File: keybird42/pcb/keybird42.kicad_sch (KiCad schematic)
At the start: 182 parts, among them SW1 SW_Push, SW10 SW_Push, SW11 SW_Push, SW12 SW_Push, SW13 SW_Push, SW14 SW_Push, SW15 SW_Push, SW16 SW_Push, SW17 SW_Push, SW18 SW_Push, SW19 SW_Push, SW2 SW_Push, SW20 SW_Push, SW21 SW_Push, SW22 SW_Push, SW23 SW_Push, SW24 SW_Push, SW25 SW_Push, SW26 SW_Push, SW27 SW_Push, SW28 SW_Push, SW29 SW_Push, SW3 SW_Push, SW30 SW_Push, SW31 SW_Push, SW32 SW_Push, SW33 SW_Push, SW34 SW_Push, SW35 SW_Push, SW36 SW_Push, SW37 SW_Push, SW38 SW_Push, SW39 SW_Push, SW4 SW_Push, SW40 SW_Push, SW41 SW_Push, SW42 SW_Push, SW43 SW_Push, SW44 SW_Push, SW45 SW_Push, SW46 SW_Push, SW47 SW_Push, SW48 SW_Push, SW49 SW_Push, SW5 SW_Push, SW50 SW_Push, SW51 SW_Push, SW52 SW_Push, SW53 SW_Push, SW54 SW_Push, SW55 SW_Push, SW56 SW_Push, SW57 SW_Push, SW58 SW_Push, SW59 SW_Push, SW6 SW_Push, SW60 SW_Push, SW61 SW_Push, SW62 SW_Push, SW63 SW_Push, SW64 SW_Push, SW65 SW_Push, SW66 SW_Push, SW67 SW_Push, SW68 SW_Push, SW69 SW_Push, SW7 SW_Push, SW70 SW_Push, SW71 SW_Push, SW72 SW_Push, SW73 SW_Push, SW74 SW_Push, SW75 SW_Push, SW76 SW_Push, SW77 SW_Push, SW78 SW_Push, SW79 SW_Push, SW8 SW_Push, SW80 SW_Push, SW81 SW_Push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

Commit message: add rp2040-tiny, fix subdir name
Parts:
- added U1: RP2040-Tiny, symbol keybird42:RP2040-Tiny
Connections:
- net COL1: now also U1.13 (GPIO13)
- net COL2: now also U1.14 (GPIO14)
- net COL3: now also U1.15 (GPIO15)
- net COL4: now also U1.16 (GPIO26)
- net COL5: now also U1.17 (GPIO27)
- net COL6: now also U1.18 (GPIO28)
- net COL7: now also U1.19 (GPIO29)
- net ROWa: now also U1.0 (GPIO0)
- net ROWb: now also U1.1 (GPIO1)
- net ROWc: now also U1.2 (GPIO2)
- net ROWd: now also U1.3 (GPIO3)
- net ROWe: now also U1.4 (GPIO4)
- net ROWf: now also U1.5 (GPIO5)
- net ROWg: now also U1.6 (GPIO6)
- net ROWh: now also U1.7 (GPIO7)
- net ROWi: now also U1.8 (GPIO8)
- net ROWj: now also U1.9 (GPIO9)
- net ROWk: now also U1.10 (GPIO10)
- net ROWl: now also U1.11 (GPIO11)
- net ROWm: now also U1.12 (GPIO12)
- new net GND: U1.21 (GND)
- no-connect marks 0 -> 2
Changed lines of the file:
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@@
   (junction (at 46.99 81.28) (diameter 0) (color 0 0 0 0)
   )
+  (no_connect (at 33.02 246.38))
+  (no_connect (at 33.02 236.22))
   (wire (pts (xy 113.03 127) (xy 127 127))
     (stroke (width 0) (type default))
@@
     (stroke (width 0) (type default))
   )
+  (label "ROWd" (at 55.88 224.79 0) (fields_autoplaced)
+    (effects (font (size 1.27 1.27)) (justify left bottom))
+  )
   (label "ROWj" (at 25.4 139.7 180) (fields_autoplaced)
     (effects (font (size 1.27 1.27)) (justify right bottom))
@@
     (effects (font (size 1.27 1.27)) (justify right bottom))
   )
+  (label "ROWl" (at 55.88 245.11 0) (fields_autoplaced)
+    (effects (font (size 1.27 1.27)) (justify left bottom))
+  )
   (label "COL2" (at 46.99 185.42 270) (fields_autoplaced)
     (effects (font (size 1.27 1.27)) (justify right bottom))
@@
     (effects (font (size 1.27 1.27)) (justify right bottom))
   )
+  (label "ROWe" (at 55.88 227.33 0) (fields_autoplaced)
+    (effects (font (size 1.27 1.27)) (justify left bottom))
+  )
   (label "ROWd" (at 25.4 63.5 180) (fields_autoplaced)
     (effects (font (size 1.27 1.27)) (justify right bottom))
@@
     (effects (font (size 1.27 1.27)) (justify right bottom))
   )
+  (label "ROWm" (at 55.88 247.65 0) (fields_autoplaced)
+    (effects (font (size 1.27 1.27)) (justify left bottom))
+  )
   (label "ROWh" (at 25.4 114.3 180) (fields_autoplaced)
     (effects (font (size 1.27 1.27)) (justify right bottom))
   )
+  (label "COL7" (at 55.88 265.43 0) (fields_autoplaced)
+    (effects (font (size 1.27 1.27)) (justify left bottom))
+  )
+  (label "ROWf" (at 55.88 229.87 0) (fields_autoplaced)
+    (effects (font (size 1.27 1.27)) (justify left bottom))
+  )
   (label "ROWk" (at 25.4 152.4 180) (fields_autoplaced)
     (effects (font (size 1.27 1.27)) (justify right bottom))
@@
     (effects (font (size 1.27 1.27)) (justify right bottom))
   )
+  (label "ROWh" (at 55.88 234.95 0) (fields_autoplaced)
+    (effects (font (size 1.27 1.27)) (justify left bottom))
+  )
   (label "ROWl" (at 25.4 165.1 180) (fields_autoplaced)
     (effects (font (size 1.27 1.27)) (justify right bottom))
@@
     (effects (font (size 1.27 1.27)) (justify right bottom))
   )
+  (label "COL6" (at 55.88 262.89 0) (fields_autoplaced)
+    (effects (font (size 1.27 1.27)) (justify left bottom))
+  )
+  (label "ROWg" (at 55.88 232.41 0) (fields_autoplaced)
+    (effects (font (size 1.27 1.27)) (justify left bottom))
+  )
+  (label "ROWa" (at 55.88 217.17 0) (fields_autoplaced)
+    (effects (font (size 1.27 1.27)) (justify left bottom))
+  )
+  (label "COL5" (at 55.88 260.35 0) (fields_autoplaced)
+    (effects (font (size 1.27 1.27)) (justify left bottom))
+  )
   (label "COL1" (at 33.02 185.42 270) (fields_autoplaced)
     (effects (font (size 1.27 1.27)) (justify right bottom))
@@
     (effects (font (size 1.27 1.27)) (justify right bottom))
   )
+  (label "COL1" (at 55.88 250.19 0) (fields_autoplaced)
+    (effects (font (size 1.27 1.27)) (justify left bottom))
+  )
+  (label "ROWk" (at 55.88 242.57 0) (fields_autoplaced)
+    (effects (font (size 1.27 1.27)) (justify left bottom))
+  )
+  (label "ROWi" (at 55.88 237.49 0) (fields_autoplaced)
+    (effects (font (size 1.27 1.27)) (justify left bottom))
+  )
+  (label "COL2" (at 55.88 252.73 0) (fields_autoplaced)
+    (effects (font (size 1.27 1.27)) (justify left bottom))
+  )
+  (label "COL3" (at 55.88 255.27 0) (fields_autoplaced)
+    (effects (font (size 1.27 1.27)) (justify left bottom))
+  )
+  (label "ROWj" (at 55.88 240.03 0) (fields_autoplaced)
+    (effects (font (size 1.27 1.27)) (justify left bottom))
+  )
+  (label "ROWc" (at 55.88 222.25 0) (fields_autoplaced)
+    (effects (font (size 1.27 1.27)) (justify left bottom))
+  )
   (label "COL3" (at 60.96 185.42 270) (fields_autoplaced)
     (effects (font (size 1.27 1.27)) (justify right bottom))
   )
+  (label "ROWb" (at 55.88 219.71 0) (fields_autoplaced)
+    (effects (font (size 1.27 1.27)) (justify left bottom))
+  )
   (label "COL6" (at 102.87 185.42 270) (fields_autoplaced)
     (effects (font (size 1.27 1.27)) (justify right bottom))
+  )
+  (label "COL4" (at 55.88 257.81 0) (fields_autoplaced)
+    (effects (font (size 1.27 1.27)) (justify left bottom))
   )
   (symbol (lib_id "Diode:1N4148W") (at 113.03 34.29 90) (unit 1)
@@
         )
       )
+    )
+  )
+  (symbol (lib_id "power:GND") (at 33.02 241.3 270) (unit 1)
+    (in_bom yes) (on_board yes) (dnp no) (fields_autoplaced)
+    (property "Reference" "#PWR01" (at 26.67 241.3 0)
+      (effects (font (size 1.27 1.27)) hide)
+    )
+    (property "Value" "GND" (at 29.21 241.3 90)
+      (effects (font (size 1.27 1.27)) (justify right))
+    )
+    (property "Footprint" "" (at 33.02 241.3 0)
+      (effects (font (size 1.27 1.27)) hide)
+    )
+    (property "Datasheet" "" (at 33.02 241.3 0)
+      (effects (font (size 1.27 1.27)) hide)
+    )
+    (pin "1")
+    (instances
+      (project "keybird42"
+        (path "/c6489b6f-cd36-4929-9d41-a438ed9c3e88"
+          (reference "#PWR01") (unit 1)
+        )
+      )
+    )
+  )
+  (symbol (lib_id "keybird42:RP2040-Tiny") (at 44.45 241.3 0) (unit 1)
+    (in_bom yes) (on_board yes) (dnp no) (fields_autoplaced)
+    (property "Reference" "U1" (at 44.45 209.55 0)
+      (effects (font (size 1.27 1.27)))
+    )
+    (property "Value" "RP2040-Tiny" (at 44.45 212.09 0)
+      (effects (font (size 1.27 1.27)))
+    )
+    (property "Footprint" "" (at 44.45 241.3 0)
+      (effects (font (size 1.27 1.27)) hide)
+    )
+    (property "Datasheet" "https://www.waveshare.com/RP2040-Tiny.htm" (at 44.45 269.24 0)
+      (effects (font (size 1.27 1.27)) hide)
+    )
+    (pin "1")
+    (pin "0")
+    (pin "19")
+    (pin "2")
+    (pin "20")
+    (pin "9")
+    (pin "7")
+    (pin "8")
+    (pin "10")
+    (pin "5")
+    (pin "4")
+    (pin "6")
+    (pin "3")
+    (pin "21")
+    (pin "22")
+    (pin "15")
+    (pin "14")
+    (pin "18")
+    (pin "16")
+    (pin "11")
+    (pin "12")
+    (pin "13")
+    (pin "17")
+    (instances
+      (project "keybird42"
+        (path "/c6489b6f-cd36-4929-9d41-a438ed9c3e88"
+          (reference "U1") (unit 1)
+        )
+      )

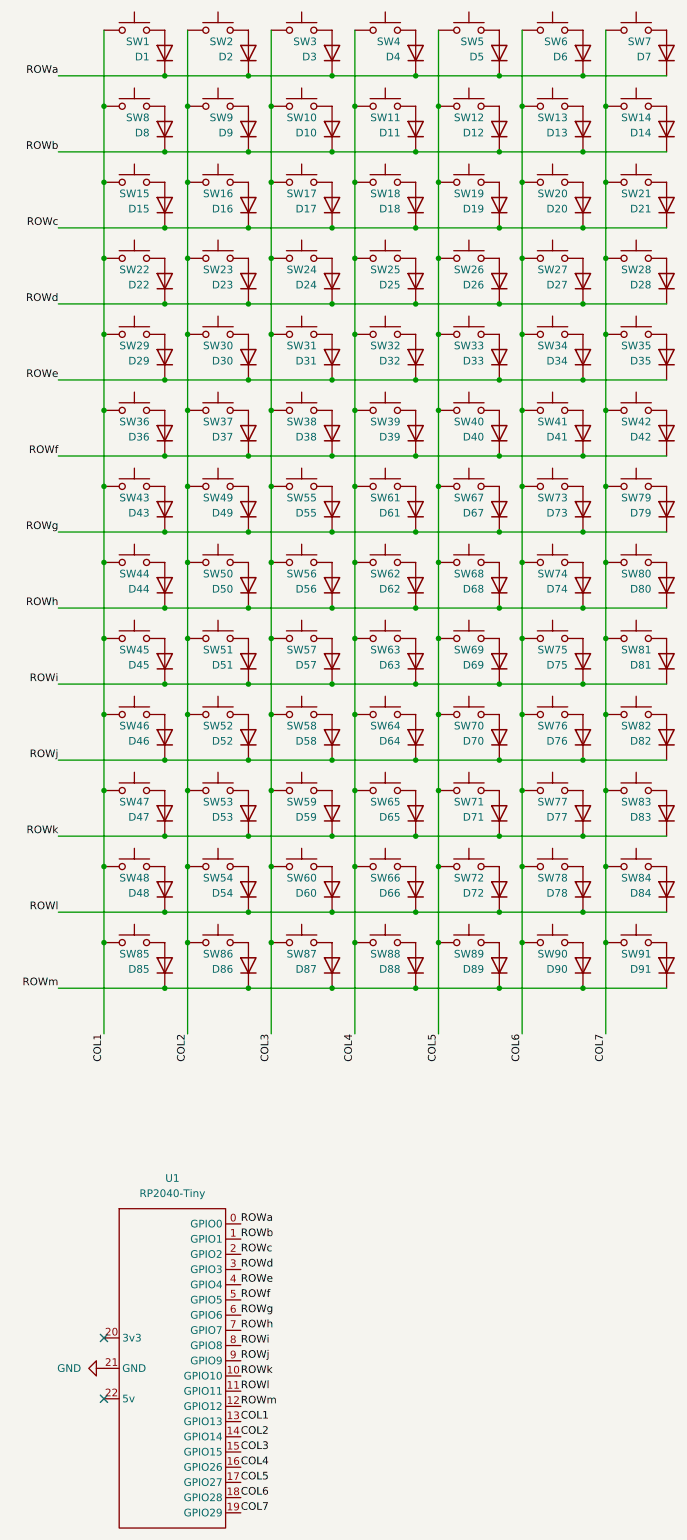
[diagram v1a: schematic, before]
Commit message: update switch and diode symbols; ERC passes; refs are a mess
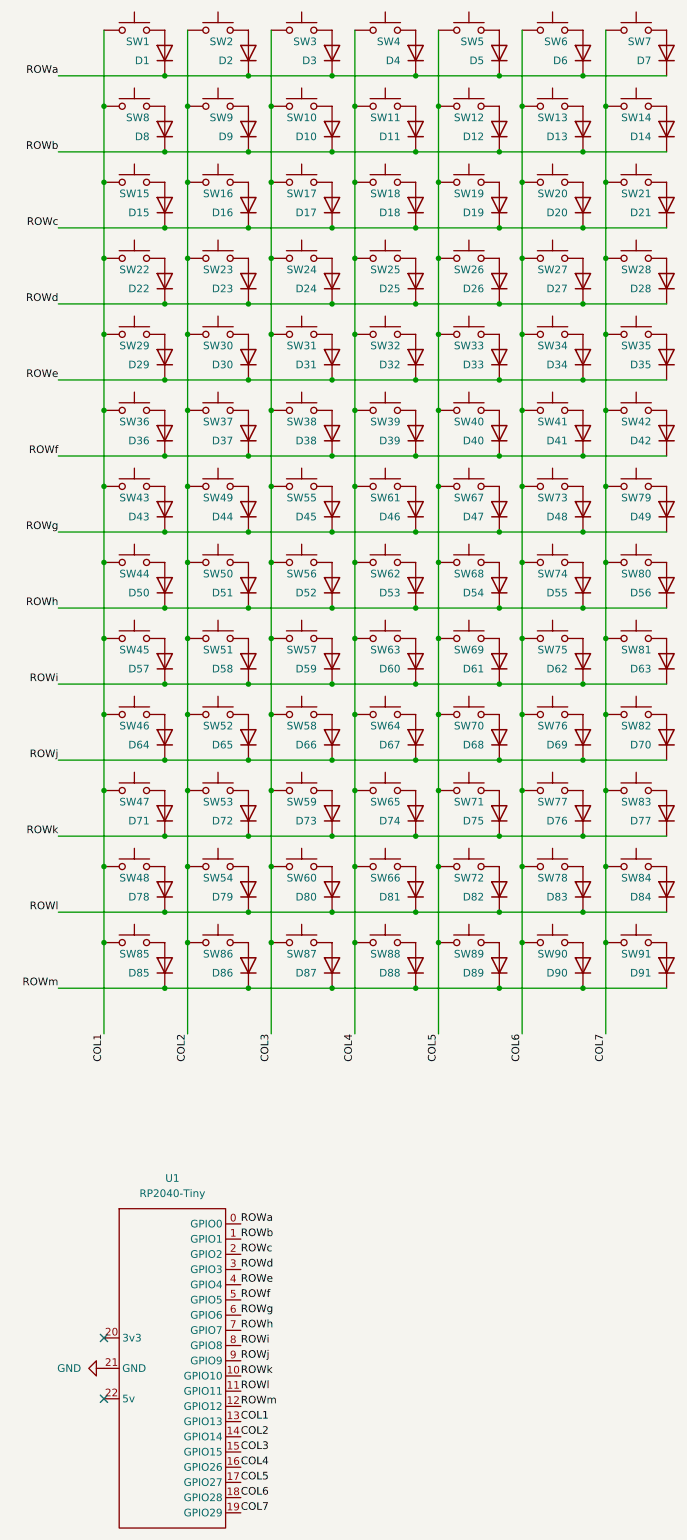
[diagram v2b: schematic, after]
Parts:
- removed D1, D10, D11, D12, D13, D14, D15, D16, D17, D18, D19, D2, D20, D21, D22, D23, D24, D25, D26, D27, D28, D29, D3, D30, D31, D32, D33, D34, D35, D36, D37, D38, D39, D4, D40, D41, D42, D43, D44, D45, D46, D47, D48, D49, D5, D50, D51, D52, D53, D54, D55, D56, D57, D58, D59, D6, D60, D61, D62, D63, D64, D65, D66, D67, D68, D69, D7, D70, D71, D72, D73, D74, D75, D76, D77, D78, D79, D8, D80, D81, D82, D83, D84, D85, D86, D87, D88, D89, D9, D90, D91: 1N4148W, Diode_SMD:D_SOD-123, symbol Diode:1N4148W
- added D1, D10, D11, D12, D13, D14, D15, D16, D17, D18, D19, D2, D20, D21, D22, D23, D24, D25, D26, D27, D28, D29, D3, D30, D31, D32, D33, D34, D35, D36, D37, D38, D39, D4, D40, D41, D42, D43, D44, D45, D46, D47, D48, D49, D5, D50, D51, D52, D53, D54, D55, D56, D57, D58, D59, D6, D60, D61, D62, D63, D64, D65, D66, D67, D68, D69, D7, D70, D71, D72, D73, D74, D75, D76, D77, D78, D79, D8, D80, D81, D82, D83, D84, D85, D86, D87, D88, D89, D9, D90, D91: 1N4148W, Diode_SMD:D_SOD-123, symbol keybird42:1N4148W
- SW1, SW10, SW11, SW12, SW13, SW14, SW15, SW16, SW17, SW18, SW19, SW2, SW20, SW21, SW22, SW23, SW24, SW25, SW26, SW27, SW28, SW29, SW3, SW30, SW31, SW32, SW33, SW34, SW35, SW36, SW37, SW38, SW39, SW4, SW40, SW41, SW42, SW43, SW44, SW45, SW46, SW47, SW48, SW49, SW5, SW50, SW51, SW52, SW53, SW54, SW55, SW56, SW57, SW58, SW59, SW6, SW60, SW61, SW62, SW63, SW64, SW65, SW66, SW67, SW68, SW69, SW7, SW70, SW71, SW72, SW73, SW74, SW75, SW76, SW77, SW78, SW79, SW8, SW80, SW81, SW82, SW83, SW84, SW85, SW86, SW87, SW88, SW89, SW9, SW90, SW91: value SW_Push -> SW_MX; footprint (none) -> PCM_Switch_Keyboard_Hotswap_Kailh:SW_Hotswap_Kailh_MX; symbol Switch:SW_Push -> keybird42:SW_MX
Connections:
- net ROWa: now also D1.1 (K), D2.1 (K), D3.1 (K), D4.1 (K), D5.1 (K), D6.1 (K), D7.1 (K)
- net ROWb: now also D10.1 (K), D11.1 (K), D12.1 (K), D13.1 (K), D14.1 (K), D8.1 (K), D9.1 (K)
- net ROWc: now also D15.1 (K), D16.1 (K), D17.1 (K), D18.1 (K), D19.1 (K), D20.1 (K), D21.1 (K)
- net ROWd: now also D22.1 (K), D23.1 (K), D24.1 (K), D25.1 (K), D26.1 (K), D27.1 (K), D28.1 (K)
- net ROWe: now also D29.1 (K), D30.1 (K), D31.1 (K), D32.1 (K), D33.1 (K), D34.1 (K), D35.1 (K)
- net ROWf: now also D36.1 (K), D37.1 (K), D38.1 (K), D39.1 (K), D40.1 (K), D41.1 (K), D42.1 (K)
- net ROWg: now also D43.1 (K), D44.1 (K), D45.1 (K), D46.1 (K), D47.1 (K), D48.1 (K), D49.1 (K)
- net ROWh: now also D50.1 (K), D51.1 (K), D52.1 (K), D53.1 (K), D54.1 (K), D55.1 (K), D56.1 (K)
- net ROWi: now also D57.1 (K), D58.1 (K), D59.1 (K), D60.1 (K), D61.1 (K), D62.1 (K), D63.1 (K)
- net ROWj: now also D64.1 (K), D65.1 (K), D66.1 (K), D67.1 (K), D68.1 (K), D69.1 (K), D70.1 (K)
- net ROWk: now also D71.1 (K), D72.1 (K), D73.1 (K), D74.1 (K), D75.1 (K), D76.1 (K), D77.1 (K)
- net ROWl: now also D78.1 (K), D79.1 (K), D80.1 (K), D81.1 (K), D82.1 (K), D83.1 (K), D84.1 (K)
- net ROWm: now also D85.1 (K), D86.1 (K), D87.1 (K), D88.1 (K), D89.1 (K), D90.1 (K), D91.1 (K)
- net at SW13.2: now also D13.2 (A)
- net at SW55.2: now also D45.2 (A)
- net at SW80.2: now also D56.2 (A)
- net at SW78.2: now also D83.2 (A)
- net at SW89.2: now also D89.2 (A)
- net at SW76.2: now also D69.2 (A)
- net at SW72.2: now also D82.2 (A)
- net at SW58.2: now also D66.2 (A)
- net at SW5.2: now also D5.2 (A)
- net at SW81.2: now also D63.2 (A)
- net at SW82.2: now also D70.2 (A)
- net at SW26.2: now also D26.2 (A)
- net at SW48.2: now also D78.2 (A)
- net at SW30.2: now also D30.2 (A)
- net at SW88.2: now also D88.2 (A)
- net at SW77.2: now also D76.2 (A)
- net at SW87.2: now also D87.2 (A)
- net at SW19.2: now also D19.2 (A)
- net at SW31.2: now also D31.2 (A)
- net at SW61.2: now also D46.2 (A)
- net at SW56.2: now also D52.2 (A)
- net at SW51.2: now also D58.2 (A)
- net at SW24.2: now also D24.2 (A)
- net at SW15.2: now also D15.2 (A)
- net at SW27.2: now also D27.2 (A)
- net at SW66.2: now also D81.2 (A)
- net at SW62.2: now also D53.2 (A)
- net at SW17.2: now also D17.2 (A)
- net at SW54.2: now also D79.2 (A)
- net at SW43.2: now also D43.2 (A)
- net at SW69.2: now also D61.2 (A)
- net at SW53.2: now also D72.2 (A)
- net at SW79.2: now also D49.2 (A)
- net at SW7.2: now also D7.2 (A)
- net at SW71.2: now also D75.2 (A)
- net at SW44.2: now also D50.2 (A)
- net at SW25.2: now also D25.2 (A)
- net at SW22.2: now also D22.2 (A)
- net at SW9.2: now also D9.2 (A)
- net at SW29.2: now also D29.2 (A)
- net at SW38.2: now also D38.2 (A)
- net at SW12.2: now also D12.2 (A)
- net at SW70.2: now also D68.2 (A)
- net at SW52.2: now also D65.2 (A)
- net at SW74.2: now also D55.2 (A)
- net at SW84.2: now also D84.2 (A)
- net at SW91.2: now also D91.2 (A)
- net at SW8.2: now also D8.2 (A)
- net at SW21.2: now also D21.2 (A)
- net at SW57.2: now also D59.2 (A)
- net at SW35.2: now also D35.2 (A)
- net at SW34.2: now also D34.2 (A)
- net at SW14.2: now also D14.2 (A)
- net at SW45.2: now also D57.2 (A)
- net at SW6.2: now also D6.2 (A)
- net at SW3.2: now also D3.2 (A)
- net at SW73.2: now also D48.2 (A)
- net at SW67.2: now also D47.2 (A)
- net at SW47.2: now also D71.2 (A)
- net at SW60.2: now also D80.2 (A)
- net at SW18.2: now also D18.2 (A)
- net at SW83.2: now also D77.2 (A)
- net at SW63.2: now also D60.2 (A)
- net at SW90.2: now also D90.2 (A)
- net at SW59.2: now also D73.2 (A)
- net at SW46.2: now also D64.2 (A)
- net at SW16.2: now also D16.2 (A)
- net at SW75.2: now also D62.2 (A)
- net at SW36.2: now also D36.2 (A)
- net at SW86.2: now also D86.2 (A)
- net at SW85.2: now also D85.2 (A)
- net at SW4.2: now also D4.2 (A)
- net at SW23.2: now also D23.2 (A)
- net at SW40.2: now also D40.2 (A)
- net at SW10.2: now also D10.2 (A)
- net at SW41.2: now also D41.2 (A)
- net at SW39.2: now also D39.2 (A)
- net at SW28.2: now also D28.2 (A)
- net at SW20.2: now also D20.2 (A)
- net at SW32.2: now also D32.2 (A)
- net at SW11.2: now also D11.2 (A)
- net at SW64.2: now also D67.2 (A)
- net at SW50.2: now also D51.2 (A)
- net at SW2.2: now also D2.2 (A)
- net at SW37.2: now also D37.2 (A)
- net at SW1.2: now also D1.2 (A)
- net at SW42.2: now also D42.2 (A)
- net at SW33.2: now also D33.2 (A)
- net at SW65.2: now also D74.2 (A)
- net at SW68.2: now also D54.2 (A)
- net at SW49.2: now also D44.2 (A)
